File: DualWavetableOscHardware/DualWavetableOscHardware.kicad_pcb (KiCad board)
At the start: 4 copper layers, 50.8 x 110 mm, 102 parts, among them J101 CV1, J102 MOD1, J103 SWD Header, J104 POWER, J105 CV2, J106 MOD2, J107 OUT1, J108 OUT2, J109 Micro_SD_Card, SW101 RST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

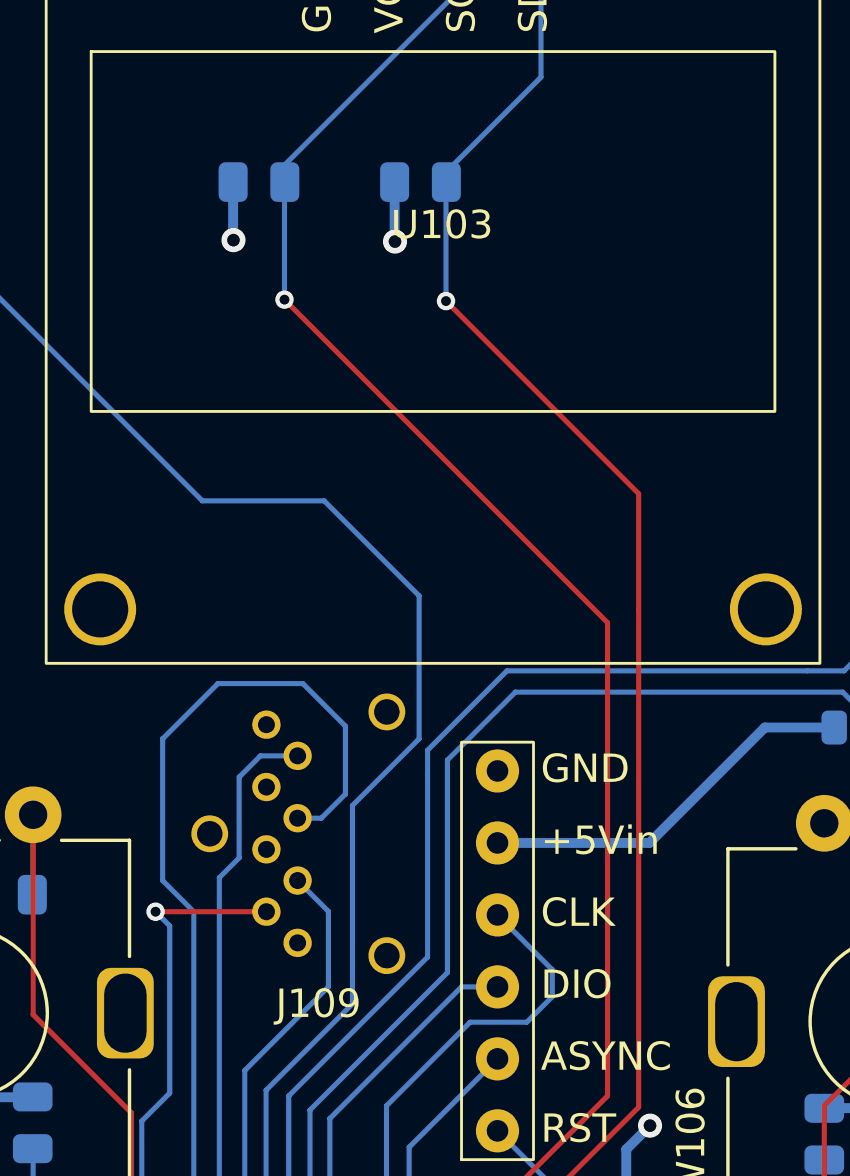
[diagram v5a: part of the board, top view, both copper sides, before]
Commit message: wavetable voice logic
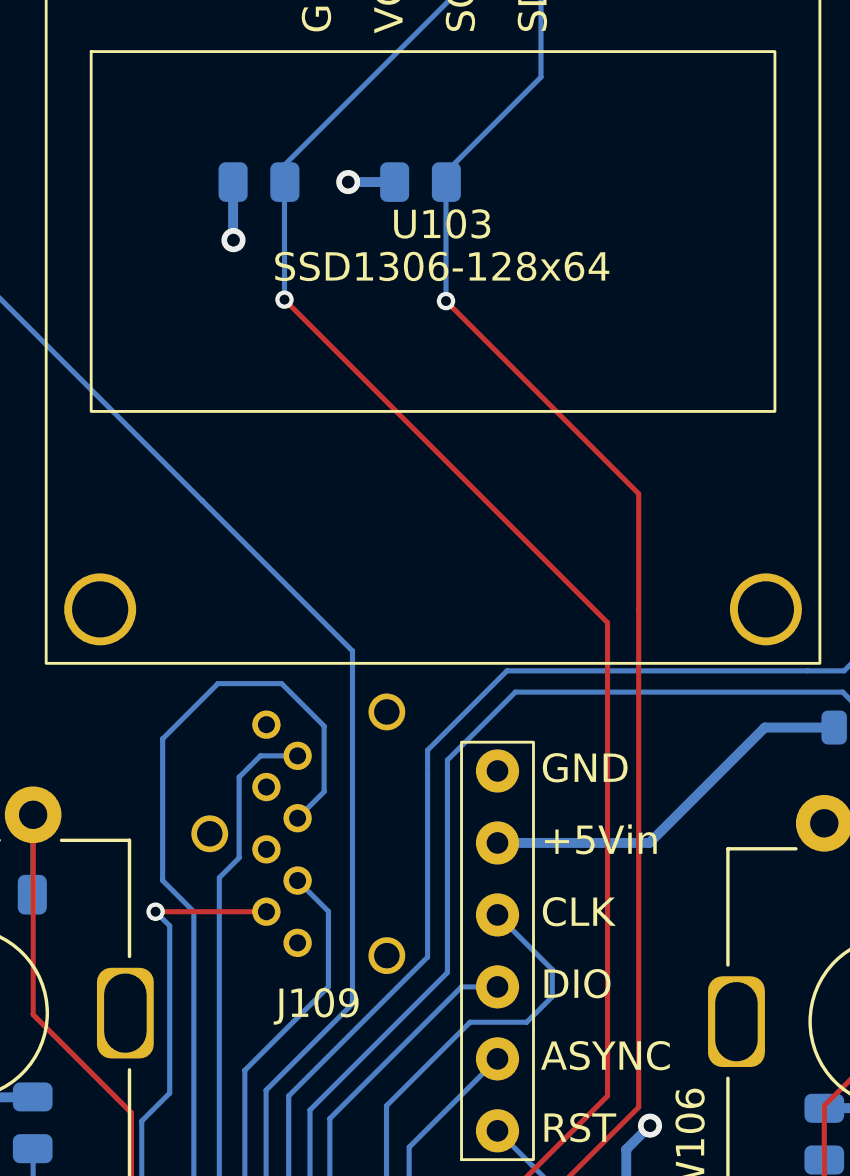
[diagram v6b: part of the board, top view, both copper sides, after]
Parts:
- U103: value ~ -> SSD1306-128x64
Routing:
- net CH_BTN: track 71.7 -> 67.2 mm
- net SCK: track 41.6 -> 40.1 mm
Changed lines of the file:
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@@
         (effects (font (size 1 1) (thickness 0.1)))
     )
-    (fp_text value "~" (at 13.97 13.97 unlocked) (layer "F.Fab")
+    (fp_text value "SSD1306-128x64" (at 13.97 13.97 unlocked) (layer "F.SilkS")
         (effects (font (size 1 1) (thickness 0.15)))
     )
-    (fp_text user "SDA" (at 17.78 2.54 90 unlocked) (layer "B.SilkS")
+    (fp_text user "GND" (at 10.16 2.54 90 unlocked) (layer "B.SilkS")
         (effects (font (size 1 1) (thickness 0.1)) (justify left bottom mirror))
     )
-    (fp_text user "VCC" (at 12.7 2.54 90 unlocked) (layer "B.SilkS")
+    (fp_text user "SCL" (at 15.24 2.54 90 unlocked) (layer "B.SilkS")
         (effects (font (size 1 1) (thickness 0.1)) (justify left bottom mirror))
     )
-    (fp_text user "GND" (at 10.16 2.54 90 unlocked) (layer "B.SilkS")
+    (fp_text user "VCC" (at 12.7 2.54 90 unlocked) (layer "B.SilkS")
         (effects (font (size 1 1) (thickness 0.1)) (justify left bottom mirror))
     )
-    (fp_text user "SCL" (at 15.24 2.54 90 unlocked) (layer "B.SilkS")
+    (fp_text user "SDA" (at 17.78 2.54 90 unlocked) (layer "B.SilkS")
         (effects (font (size 1 1) (thickness 0.1)) (justify left bottom mirror))
     )
-    (fp_text user "SDA" (at 17.78 5.715 90 unlocked) (layer "F.SilkS")
+    (fp_text user "VCC" (at 12.7 5.715 90 unlocked) (layer "F.SilkS")
         (effects (font (size 1 1) (thickness 0.1)) (justify left bottom))
     )
-    (fp_text user "GND" (at 10.16 5.715 90 unlocked) (layer "F.SilkS")
+    (fp_text user "SDA" (at 17.78 5.715 90 unlocked) (layer "F.SilkS")
         (effects (font (size 1 1) (thickness 0.1)) (justify left bottom))
     )
-    (fp_text user "VCC" (at 12.7 5.715 90 unlocked) (layer "F.SilkS")
+    (fp_text user "SCL" (at 15.24 5.715 90 unlocked) (layer "F.SilkS")
         (effects (font (size 1 1) (thickness 0.1)) (justify left bottom))
     )
-    (fp_text user "SCL" (at 15.24 5.715 90 unlocked) (layer "F.SilkS")
+    (fp_text user "GND" (at 10.16 5.715 90 unlocked) (layer "F.SilkS")
         (effects (font (size 1 1) (thickness 0.1)) (justify left bottom))
     )
@@
     (pad "4" thru_hole circle locked (at 17.4625 1.27) (size 1.524 1.524) (drill 0.762) (layers "*.Cu" "*.Mask")
       (net 31 "SDA") (pinfunction "SDA") (pintype "input"))
-    (group "" (id c563db7a-997f-4ae5-a5dc-dc10bc758b21)
+    (group "" (id bd0a3c81-e1c4-4111-a2f5-2219e1042bca)
       (members
-        01024df2-1610-4ea6-9291-5c6ce8998396
-        2f760e54-e4f5-42fa-88ff-813d83eeb67e
-        38a8e1ad-6c5f-4d29-994c-cd69a40842e5
-        a3782b08-7f6e-4340-91ab-594db1950187
+        5cfd6367-69b2-4389-9966-541f2be23a3d
+        d5c0c04e-37f1-470f-832d-bc5da194648f
+        ec294b92-427c-41b8-8568-dad082593fd0
+        f9009efc-2345-4181-b9fb-d9c4fa89c9a1
       )
     )
@@
   (via (at 23.15 52.4) (size 0.85) (drill 0.45) (layers "F.Cu" "B.Cu") (net 4))
   (via (at 30.6 59.45) (size 0.85) (drill 0.45) (layers "F.Cu" "B.Cu") (net 4))
-  (via (at 24.5 13.6) (size 0.85) (drill 0.45) (layers "F.Cu" "B.Cu") (net 4))
+  (via (at 22.85 11.5) (size 0.85) (drill 0.45) (layers "F.Cu" "B.Cu") (net 4))
   (via (at 18.8 13.55) (size 0.85) (drill 0.45) (layers "F.Cu" "B.Cu") (net 4))
   (via (at 42 44.2) (size 0.8) (drill 0.4) (layers "F.Cu" "B.Cu") (net 4))
@@
   (segment (start 29.501212 61.248788) (end 30.25 60.5) (width 0.2) (layer "B.Cu") (net 4))
   (segment (start 43.4 51.25) (end 45.15 51.25) (width 0.35) (layer "B.Cu") (net 4))
-  (segment (start 24.4875 11.5) (end 24.4875 13.5875) (width 0.35) (layer "B.Cu") (net 4))
   (segment (start 37.95 98.179) (end 39.159 99.388) (width 0.35) (layer "B.Cu") (net 4))
   (segment (start 19.712124 61.248788) (end 19.063336 60.6) (width 0.2) (layer "B.Cu") (net 4))
@@
   (segment (start 41.9825 44.1825) (end 39.655 44.1825) (width 0.35) (layer "B.Cu") (net 4))
   (segment (start 13.7375 50.1625) (end 13.75 50.15) (width 0.35) (layer "B.Cu") (net 4))
+  (segment (start 24.4875 11.5) (end 22.85 11.5) (width 0.35) (layer "B.Cu") (net 4))
   (segment (start 24.028249 53.278249) (end 23.15 52.4) (width 0.2) (layer "B.Cu") (net 4))
   (segment (start 37.95 96.95) (end 37.95 98.179) (width 0.35) (layer "B.Cu") (net 4))
-  (segment (start 24.4875 13.5875) (end 24.5 13.6) (width 0.35) (layer "B.Cu") (net 4))
   (segment (start 48.8125 35.8875) (end 48.8 35.9) (width 0.35) (layer "B.Cu") (net 4))
   (segment (start 23.601212 53.748788) (end 24.028249 53.321751) (width 0.2) (layer "B.Cu") (net 4))
@@
   (segment (start 16.55 43.65) (end 16.55 37.75) (width 0.18) (layer "B.Cu") (net 50))
   (segment (start 16.55 37.75) (end 16.05 37.25) (width 0.18) (layer "B.Cu") (net 50))
-  (segment (start 18.25 29.2) (end 21.25 29.2) (width 0.18) (layer "B.Cu") (net 51))
-  (segment (start 22.75 30.7) (end 22.75 33.1) (width 0.18) (layer "B.Cu") (net 51))
+  (segment (start 22 30.7) (end 20.5 29.2) (width 0.18) (layer "B.Cu") (net 51))
   (segment (start 17.4 56.23198) (end 17.4 37.25) (width 0.18) (layer "B.Cu") (net 51))
   (segment (start 16.3 31.15) (end 18.25 29.2) (width 0.18) (layer "B.Cu") (net 51))
-  (segment (start 22.75 33.1) (end 21.9 33.95) (width 0.18) (layer "B.Cu") (net 51))
-  (segment (start 21.9 33.95) (end 21.0625 33.95) (width 0.18) (layer "B.Cu") (net 51))
-  (segment (start 21.25 29.2) (end 22.75 30.7) (width 0.18) (layer "B.Cu") (net 51))
+  (segment (start 21.0625 33.95) (end 22 33.0125) (width 0.18) (layer "B.Cu") (net 51))
+  (segment (start 18.25 29.2) (end 20.5 29.2) (width 0.18) (layer "B.Cu") (net 51))
   (segment (start 16.3 36.15) (end 16.3 31.15) (width 0.18) (layer "B.Cu") (net 51))
   (segment (start 20.065678 58.897658) (end 17.4 56.23198) (width 0.18) (layer "B.Cu") (net 51))
+  (segment (start 22 33.0125) (end 22 30.7) (width 0.18) (layer "B.Cu") (net 51))
   (segment (start 17.4 37.25) (end 16.3 36.15) (width 0.18) (layer "B.Cu") (net 51))
   (segment (start 18.3 36.05) (end 19 35.35) (width 0.18) (layer "B.Cu") (net 52))
@@
   (segment (start 22.275 90.935) (end 21.933604 90.935) (width 0.2) (layer "B.Cu") (net 61))
   (segment (start 22.3125 83.5625) (end 22.35 83.6) (width 0.2) (layer "B.Cu") (net 61))
-  (segment (start 19.95 56.66066) (end 19.95 43.55) (width 0.18) (layer "B.Cu") (net 66))
   (segment (start 17.7 22.75) (end 8.15 13.2) (width 0.18) (layer "B.Cu") (net 66))
   (segment (start 19.95 43.55) (end 23 40.5) (width 0.18) (layer "B.Cu") (net 66))
@@
   (segment (start 8.15 13.2) (end 3.4375 13.2) (width 0.18) (layer "B.Cu") (net 66))
   (segment (start 3.4375 13.2) (end 3.4 13.2375) (width 0.18) (layer "B.Cu") (net 66))
-  (segment (start 22 22.75) (end 17.7 22.75) (width 0.18) (layer "B.Cu") (net 66))
   (segment (start 3.41 9.83) (end 3.41 3.33) (width 0.18) (layer "B.Cu") (net 66))
-  (segment (start 25.35 26.1) (end 22 22.75) (width 0.18) (layer "B.Cu") (net 66))
-  (segment (start 23 33.5) (end 25.35 31.15) (width 0.18) (layer "B.Cu") (net 66))
-  (segment (start 23 40.5) (end 23 33.5) (width 0.18) (layer "B.Cu") (net 66))
-  (segment (start 25.35 31.15) (end 25.35 26.1) (width 0.18) (layer "B.Cu") (net 66))
+  (segment (start 19.95 56.66066) (end 19.95 43.55) (width 0.18) (layer "B.Cu") (net 66))
+  (segment (start 23 40.5) (end 23 28.05) (width 0.18) (layer "B.Cu") (net 66))
+  (segment (start 23 28.05) (end 17.7 22.75) (width 0.18) (layer "B.Cu") (net 66))
   (segment (start 3.41 13.2275) (end 3.41 9.83) (width 0.18) (layer "B.Cu") (net 66))
   (segment (start 21.126338 57.836998) (end 19.95 56.66066) (width 0.18) (layer "B.Cu") (net 66))
